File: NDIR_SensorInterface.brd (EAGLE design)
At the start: 26 x 49.7 mm, 2 parts, among them J1 CONN_I2C_SENSOR_BOARD_MOUNT_T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, J2 CONN_42.54

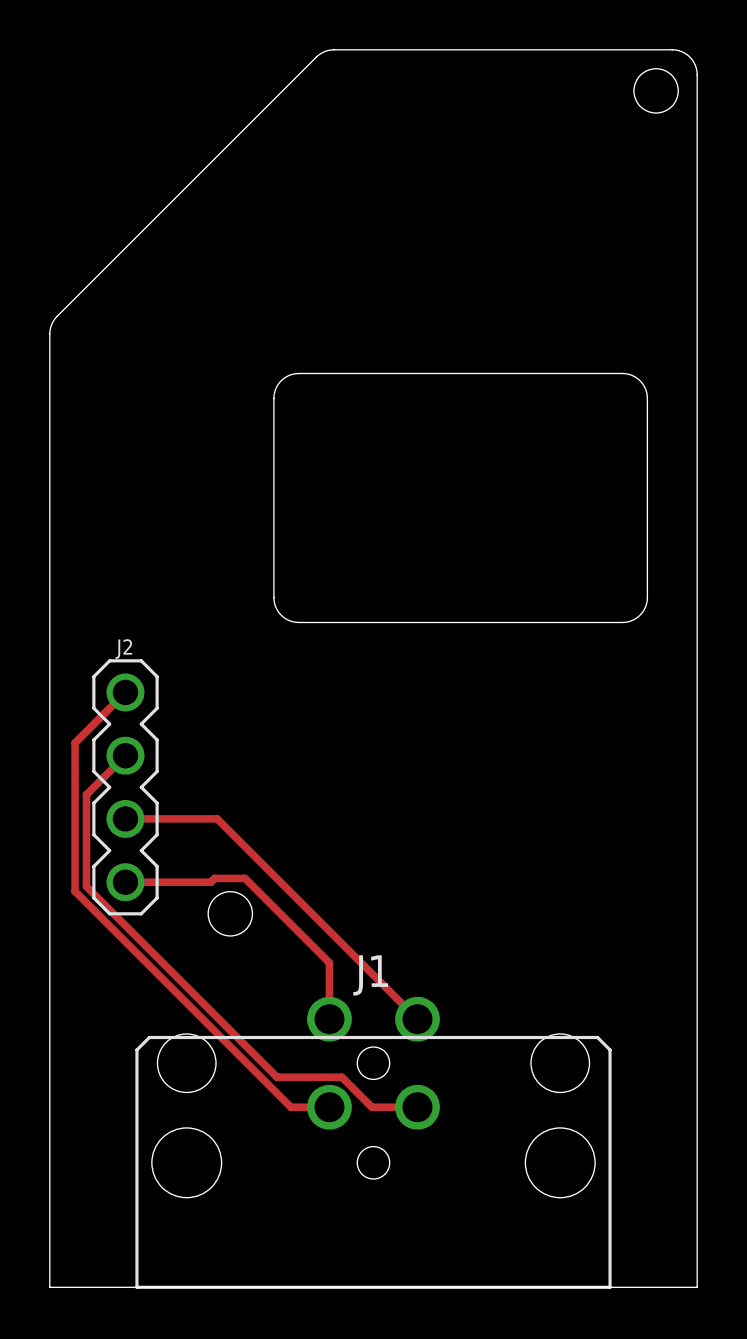
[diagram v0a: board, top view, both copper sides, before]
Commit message: Fixed hole placement
Adjusted the placement of the holes and cutout to fix errors
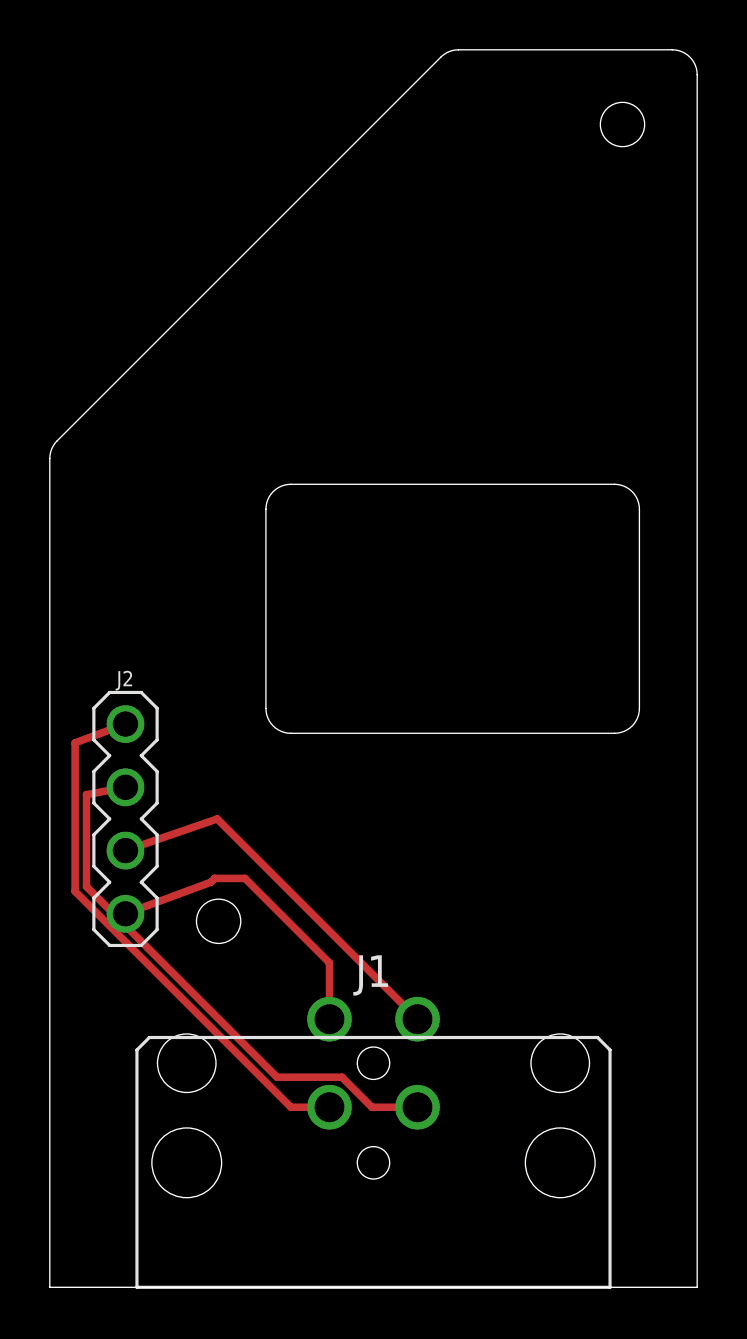
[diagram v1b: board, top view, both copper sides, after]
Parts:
- moved J2 1.27 mm to (3.04, 18.8)
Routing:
- net SDA: track 22.6 -> 21.9 mm
- net SCL: track 22.9 -> 22.3 mm
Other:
- outline, holes or cut-outs redrawn
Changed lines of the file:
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@@
 <grid distance="50" unitdist="mil" unit="mm" style="lines" multiple="1" display="no" altdistance="5" altunitdist="mil" altunit="mm"/>
 <layers>
-<layer number="1" name="Top" color="4" fill="1" visible="yes" active="yes"/>
+<layer number="1" name="Top" color="4" fill="1" visible="no" active="yes"/>
 <layer number="2" name="Route2" color="16" fill="1" visible="no" active="no"/>
 <layer number="3" name="Route3" color="17" fill="1" visible="no" active="no"/>
@@
 <layer number="14" name="Route14" color="22" fill="1" visible="no" active="no"/>
 <layer number="15" name="Route15" color="23" fill="1" visible="no" active="no"/>
-<layer number="16" name="Bottom" color="1" fill="1" visible="yes" active="yes"/>
+<layer number="16" name="Bottom" color="1" fill="1" visible="no" active="yes"/>
 <layer number="17" name="Pads" color="2" fill="1" visible="yes" active="yes"/>
-<layer number="18" name="Vias" color="2" fill="1" visible="yes" active="yes"/>
+<layer number="18" name="Vias" color="2" fill="1" visible="no" active="yes"/>
 <layer number="19" name="Unrouted" color="6" fill="1" visible="yes" active="yes"/>
 <layer number="20" name="Dimension" color="24" fill="1" visible="yes" active="yes"/>
-<layer number="21" name="tPlace" color="7" fill="1" visible="yes" active="yes"/>
-<layer number="22" name="bPlace" color="7" fill="1" visible="yes" active="yes"/>
+<layer number="21" name="tPlace" color="7" fill="1" visible="no" active="yes"/>
+<layer number="22" name="bPlace" color="7" fill="1" visible="no" active="yes"/>
 <layer number="23" name="tOrigins" color="15" fill="1" visible="yes" active="yes"/>
 <layer number="24" name="bOrigins" color="15" fill="1" visible="yes" active="yes"/>
-<layer number="25" name="tNames" color="7" fill="1" visible="yes" active="yes"/>
-<layer number="26" name="bNames" color="7" fill="1" visible="yes" active="yes"/>
-<layer number="27" name="tValues" color="7" fill="1" visible="yes" active="yes"/>
-<layer number="28" name="bValues" color="7" fill="1" visible="yes" active="yes"/>
+<layer number="25" name="tNames" color="7" fill="1" visible="no" active="yes"/>
+<layer number="26" name="bNames" color="7" fill="1" visible="no" active="yes"/>
+<layer number="27" name="tValues" color="7" fill="1" visible="no" active="yes"/>
+<layer number="28" name="bValues" color="7" fill="1" visible="no" active="yes"/>
 <layer number="29" name="tStop" color="7" fill="3" visible="no" active="yes"/>
 <layer number="30" name="bStop" color="7" fill="6" visible="no" active="yes"/>
@@
 <layer number="50" name="dxf" color="7" fill="1" visible="no" active="no"/>
 <layer number="51" name="tDocu" color="7" fill="1" visible="yes" active="yes"/>
-<layer number="52" name="bDocu" color="7" fill="1" visible="yes" active="yes"/>
+<layer number="52" name="bDocu" color="7" fill="1" visible="no" active="yes"/>
 <layer number="53" name="tGND_GNDA" color="7" fill="1" visible="no" active="no"/>
 <layer number="54" name="bGND_GNDA" color="7" fill="1" visible="no" active="no"/>
@@
 <plain>
 <wire x1="0" y1="0" x2="26" y2="0" width="0" layer="20"/>
-<wire x1="11.4142125" y1="49.7" x2="25" y2="49.7" width="0" layer="20"/>
+<wire x1="0" y1="0" x2="0" y2="33.2857875" width="0" layer="20"/>
+<wire x1="0" y1="33.2857875" x2="0.29289375" y2="33.99289375" width="0" layer="20" curve="-45"/>
+<wire x1="0.29289375" y1="33.99289375" x2="15.70710625" y2="49.40710625" width="0" layer="20"/>
+<wire x1="15.70710625" y1="49.40710625" x2="16.4142125" y2="49.7" width="0" layer="20" curve="-45"/>
+<wire x1="16.4142125" y1="49.7" x2="25" y2="49.7" width="0" layer="20"/>
 <wire x1="25" y1="49.7" x2="26" y2="48.7" width="0" layer="20" curve="-90"/>
 <wire x1="26" y1="48.7" x2="26" y2="0" width="0" layer="20"/>
-<wire x1="0.29289375" y1="38.99289375" x2="10.70710625" y2="49.40710625" width="0" layer="20"/>
-<wire x1="10.70710625" y1="49.40710625" x2="11.4142125" y2="49.7" width="0" layer="20" curve="-45"/>
-<wire x1="0" y1="0" x2="0" y2="38.2857875" width="0" layer="20"/>
-<wire x1="0" y1="38.2857875" x2="0.29289375" y2="38.99289375" width="0" layer="20" curve="-45"/>
-<wire x1="9" y1="27.7" x2="9" y2="35.7" width="0" layer="20"/>
-<wire x1="9" y1="35.7" x2="10" y2="36.7" width="0" layer="20" curve="-90"/>
-<wire x1="10" y1="36.7" x2="23" y2="36.7" width="0" layer="20"/>
-<wire x1="23" y1="36.7" x2="24" y2="35.7" width="0" layer="20" curve="-90"/>
-<wire x1="24" y1="35.7" x2="24" y2="27.7" width="0" layer="20"/>
-<wire x1="24" y1="27.7" x2="23" y2="26.7" width="0" layer="20" curve="-90"/>
-<wire x1="23" y1="26.7" x2="10" y2="26.7" width="0" layer="20"/>
-<wire x1="10" y1="26.7" x2="9" y2="27.7" width="0" layer="20" curve="-90"/>
-<hole x="24.35" y="48.05" drill="1.778"/>
-<hole x="7.25" y="15" drill="1.778"/>
+<wire x1="22.68" y1="22.25" x2="9.68" y2="22.25" width="0" layer="20"/>
+<wire x1="9.68" y1="22.25" x2="8.68" y2="23.25" width="0" layer="20" curve="-90"/>
+<wire x1="8.68" y1="23.25" x2="8.68" y2="31.25" width="0" layer="20"/>
+<wire x1="8.68" y1="31.25" x2="9.68" y2="32.25" width="0" layer="20" curve="-90"/>
+<wire x1="9.68" y1="32.25" x2="22.68" y2="32.25" width="0" layer="20"/>
+<wire x1="22.68" y1="32.25" x2="23.68" y2="31.25" width="0" layer="20" curve="-90"/>
+<wire x1="23.68" y1="31.25" x2="23.68" y2="23.25" width="0" layer="20"/>
+<wire x1="23.68" y1="23.25" x2="22.68" y2="22.25" width="0" layer="20" curve="-90"/>
+<hole x="23" y="46.7" drill="1.778"/>
+<hole x="6.78" y="14.7" drill="1.778"/>
 <text x="25.4" y="41.91" size="1.778" layer="52" font="vector" ratio="15" rot="MR0" align="center-left">Project Hedorah
 NDIR - SCD30
 v0.0</text>
-<text x="5.08" y="22.86" size="0.8128" layer="51" font="vector" ratio="15" align="center-left">Creature of Slime and Sludge
+<text x="5.08" y="18.796" size="0.8128" layer="51" font="vector" ratio="15" align="center-left">Creature of Slime and Sludge
 Spawned by Pollution's Poison
 Threatens to Destroy the Earth!</text>
@@
 <attribute name="NAME" x="13" y="12.7" size="1.27" layer="25" font="vector" ratio="15" rot="R180" align="center"/>
 </element>
-<element name="J2" library="bschulz" package="1X04" value="CONN_42.54" x="3.04" y="20.08" smashed="yes" rot="R90">
-<attribute name="NAME" x="2.681" y="25.408" size="0.6096" layer="25" font="vector" ratio="20"/>
-<attribute name="VALUE" x="5.072" y="16.27" size="0.6096" layer="27" font="vector" ratio="20" rot="R90"/>
+<element name="J2" library="bschulz" package="1X04" value="CONN_42.54" x="3.04" y="18.81" smashed="yes" rot="R90">
+<attribute name="NAME" x="2.681" y="24.138" size="0.6096" layer="25" font="vector" ratio="20"/>
+<attribute name="VALUE" x="5.072" y="15" size="0.6096" layer="27" font="vector" ratio="20" rot="R90"/>
 </element>
 </elements>
@@
 <wire x1="11.232234375" y1="13.029346875" x2="7.83918125" y2="16.4224" width="0.3048" layer="1"/>
 <wire x1="6.6214" y1="16.4224" x2="6.469" y2="16.27" width="0.3048" layer="1"/>
-<wire x1="6.469" y1="16.27" x2="3.04" y2="16.27" width="0.3048" layer="1"/>
+<wire x1="6.469" y1="16.27" x2="3.04" y2="15" width="0.3048" layer="1"/>
 <wire x1="7.83918125" y1="16.4224" x2="6.6214" y2="16.4224" width="0.3048" layer="1"/>
 </signal>
@@
 <contactref element="J1" pad="1"/>
 <wire x1="14.767765625" y1="10.767765625" x2="6.72553125" y2="18.81" width="0.3048" layer="1"/>
-<wire x1="6.72553125" y1="18.81" x2="3.04" y2="18.81" width="0.3048" layer="1"/>
+<wire x1="6.72553125" y1="18.81" x2="3.04" y2="17.54" width="0.3048" layer="1"/>
 </signal>
 <signal name="SCL">
@@
 <wire x1="14.767765625" y1="7.232234375" x2="12.936078125" y2="7.232234375" width="0.3048" layer="1"/>
 <wire x1="12.936078125" y1="7.232234375" x2="11.73128125" y2="8.43703125" width="0.3048" layer="1"/>
-<wire x1="1.4732" y1="19.7832" x2="3.04" y2="21.35" width="0.3048" layer="1"/>
+<wire x1="1.4732" y1="19.7832" x2="3.04" y2="20.08" width="0.3048" layer="1"/>
 <wire x1="11.73128125" y1="8.43703125" x2="9.12559375" y2="8.43703125" width="0.3048" layer="1"/>
 <wire x1="9.12559375" y1="8.43703125" x2="1.4732" y2="16.089425" width="0.3048" layer="1"/>
@@
 <wire x1="11.232234375" y1="7.232234375" x2="9.683809375" y2="7.232234375" width="0.3048" layer="1"/>
 <wire x1="9.683809375" y1="7.232234375" x2="1.016" y2="15.90004375" width="0.3048" layer="1"/>
-<wire x1="1.016" y1="21.866" x2="3.04" y2="23.89" width="0.3048" layer="1"/>
+<wire x1="1.016" y1="21.866" x2="3.04" y2="22.62" width="0.3048" layer="1"/>
 <wire x1="1.016" y1="15.90004375" x2="1.016" y2="21.866" width="0.3048" layer="1"/>
 </signal>

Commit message: Updated NDIR interface board to v1.0
Added reverse polarity protection and I2C pull up resistors
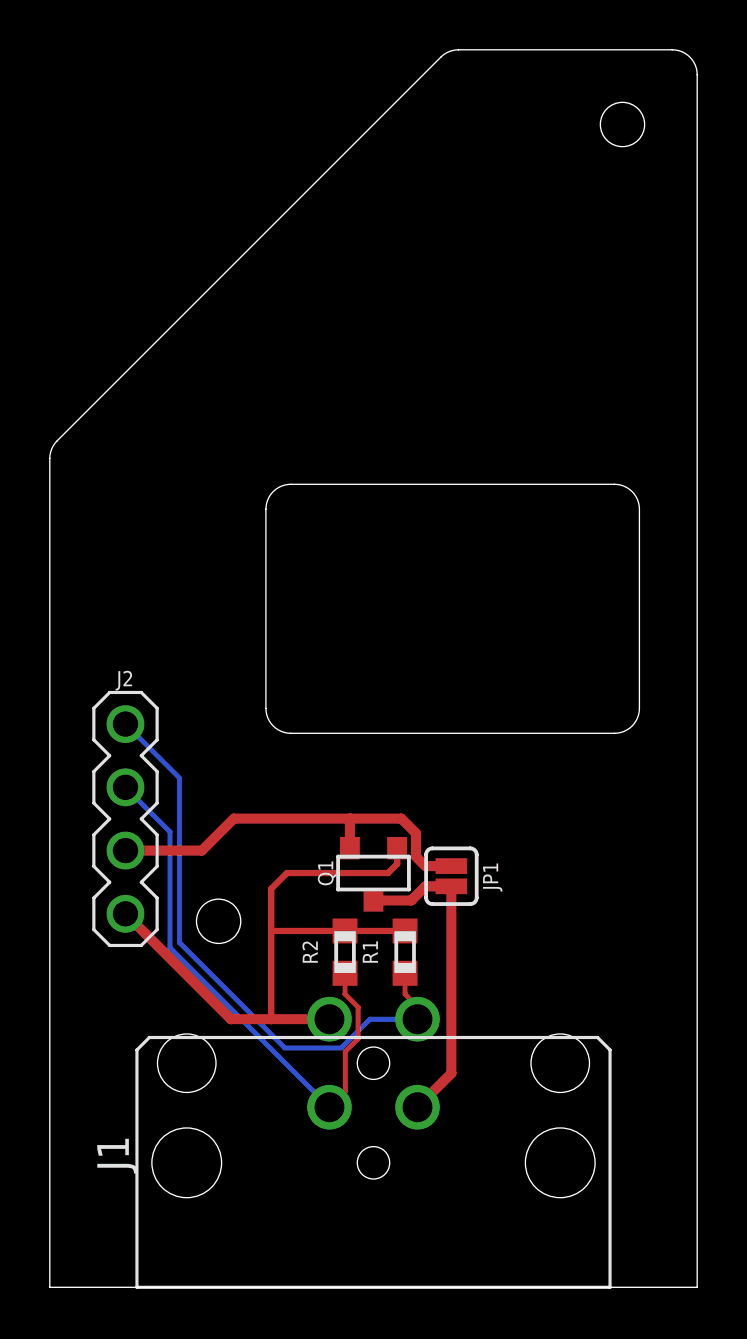
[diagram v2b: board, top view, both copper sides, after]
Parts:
- added JP1: JUMPER-SMT_2_NO_SILK, bschulz:SMT-JUMPER_2_NO_SILK
- added Q1: DMG3404, bschulz:SOT23-3
- added R1, R2: 10k, bschulz_passives:R0603
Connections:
- removed net 3V3: J1.2, J2.1
- new net VIN+: J1.2, J2.1, Q1.1, R1.2, R2.2
- new net VIN-: J1.4, JP1.1, Q1.3
- net GND: now also JP1.2, Q1.2; no longer J1.1
- net SCL: now also J1.3, R2.1; no longer J1.4
- net SDA: now also J1.1, R1.1; no longer J1.3
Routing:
- net VIN+: track 0.00 -> 26.7 mm
- net VIN-: track 0.00 -> 12.8 mm
- net 3V3: track 12.2 -> 0.00 mm
- net SDA: track 21.9 -> 23.5 mm
- net GND: track 15.3 -> 16.2 mm
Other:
- board text added: "Project Hedorah NDIR - SCD30 v1.0"
- board text removed: "Project Hedorah NDIR - SCD30 v0.0"
